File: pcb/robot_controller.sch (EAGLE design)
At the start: 93 parts, among them IC2 ESP32-DEVKIT, IC3 BTS7960B, IC4 BTS7960B, IC5 BTS7960B, IC6 BTS7960B, IC7 BTS7960B, IC8 BTS7960B, J6 1X2-3.5MM, Q1 IRLB8743

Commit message: update PCB to v1.1
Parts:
- added C43: (no value), rcl:CPOL-EUE5-10.5
- C42: value 10nF -> 100nF
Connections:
- removed net A13: IC2.D25
- removed net N$8: IC2.D35
- net GND: now also C43.-
- net VBATT: now also C43.+
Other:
- moved on the sheet: C42, R18, R20

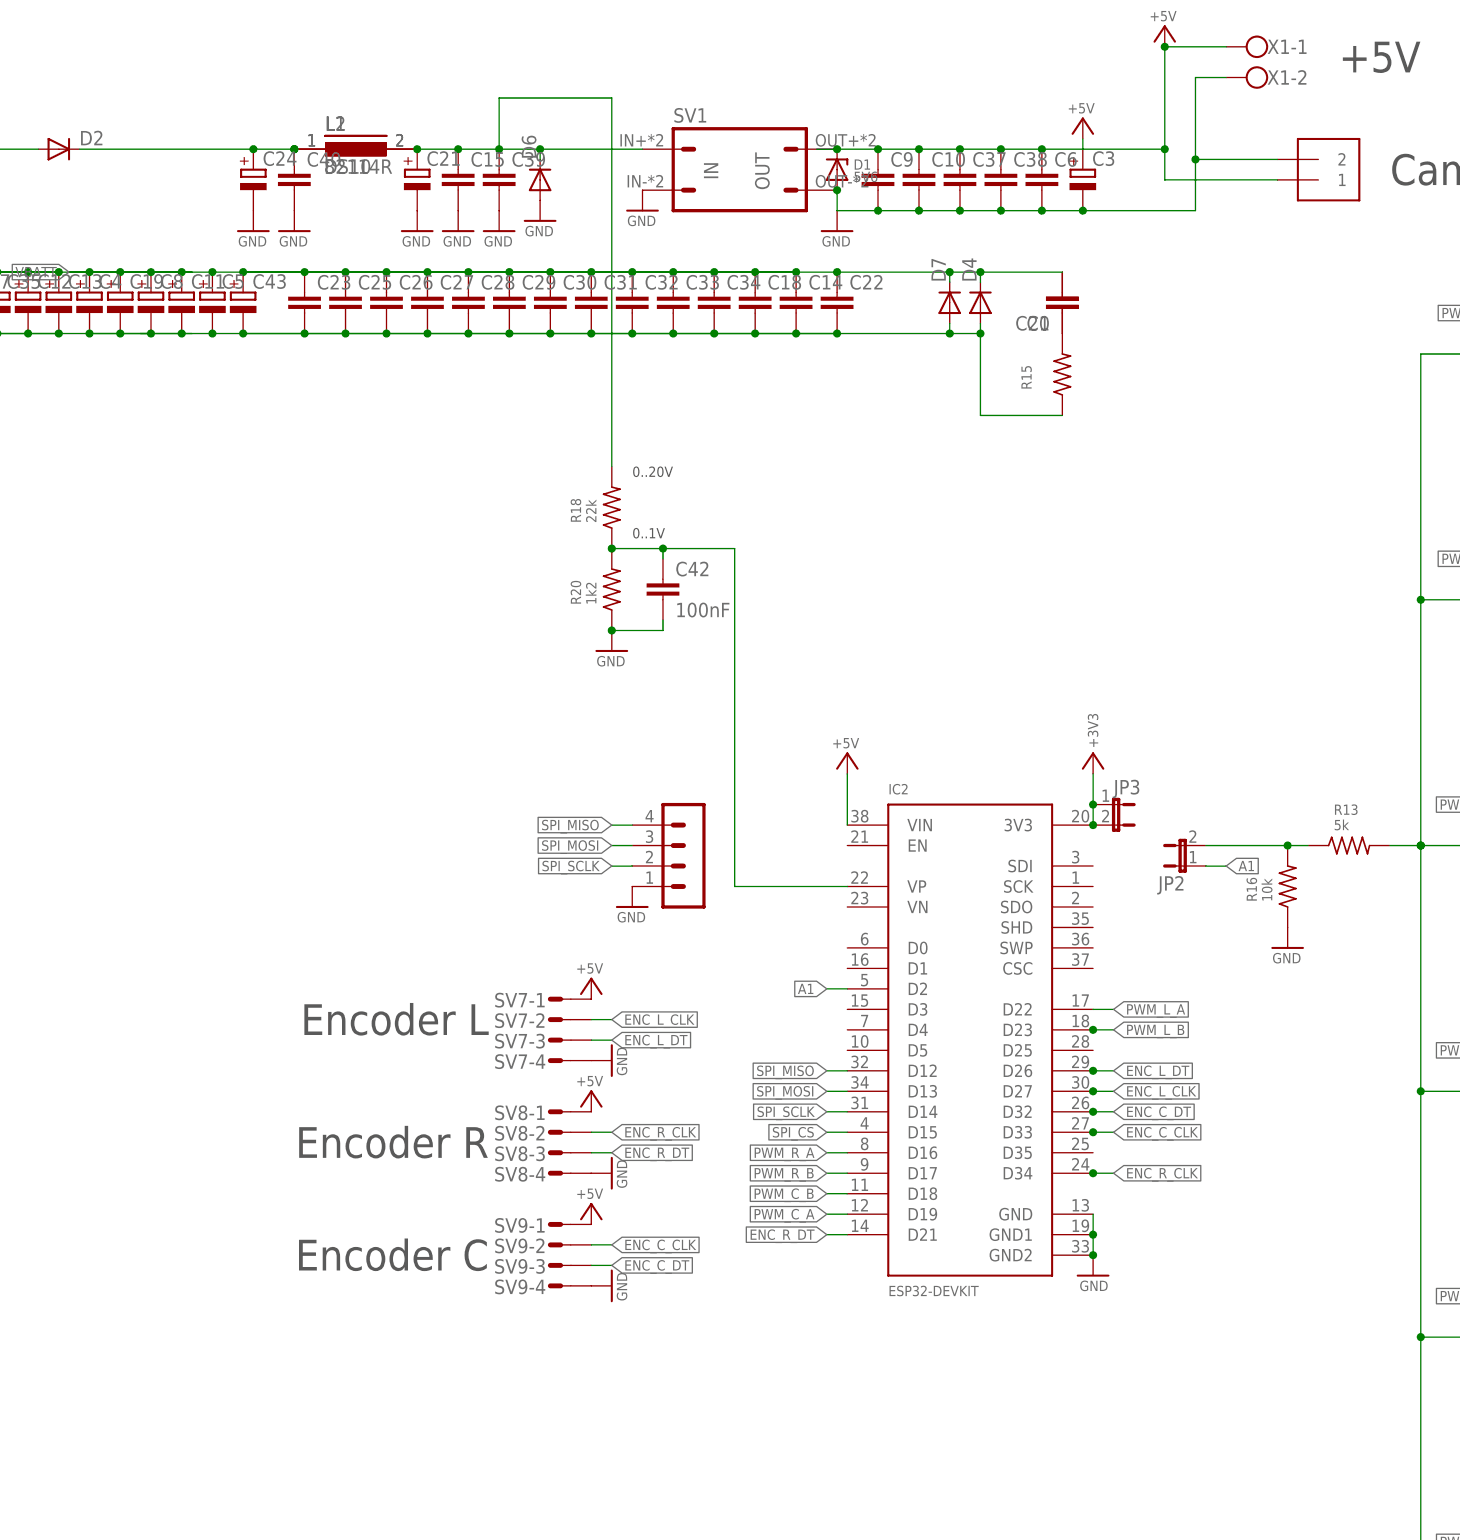
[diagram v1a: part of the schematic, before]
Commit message: update PCB and gerbers for v1.1
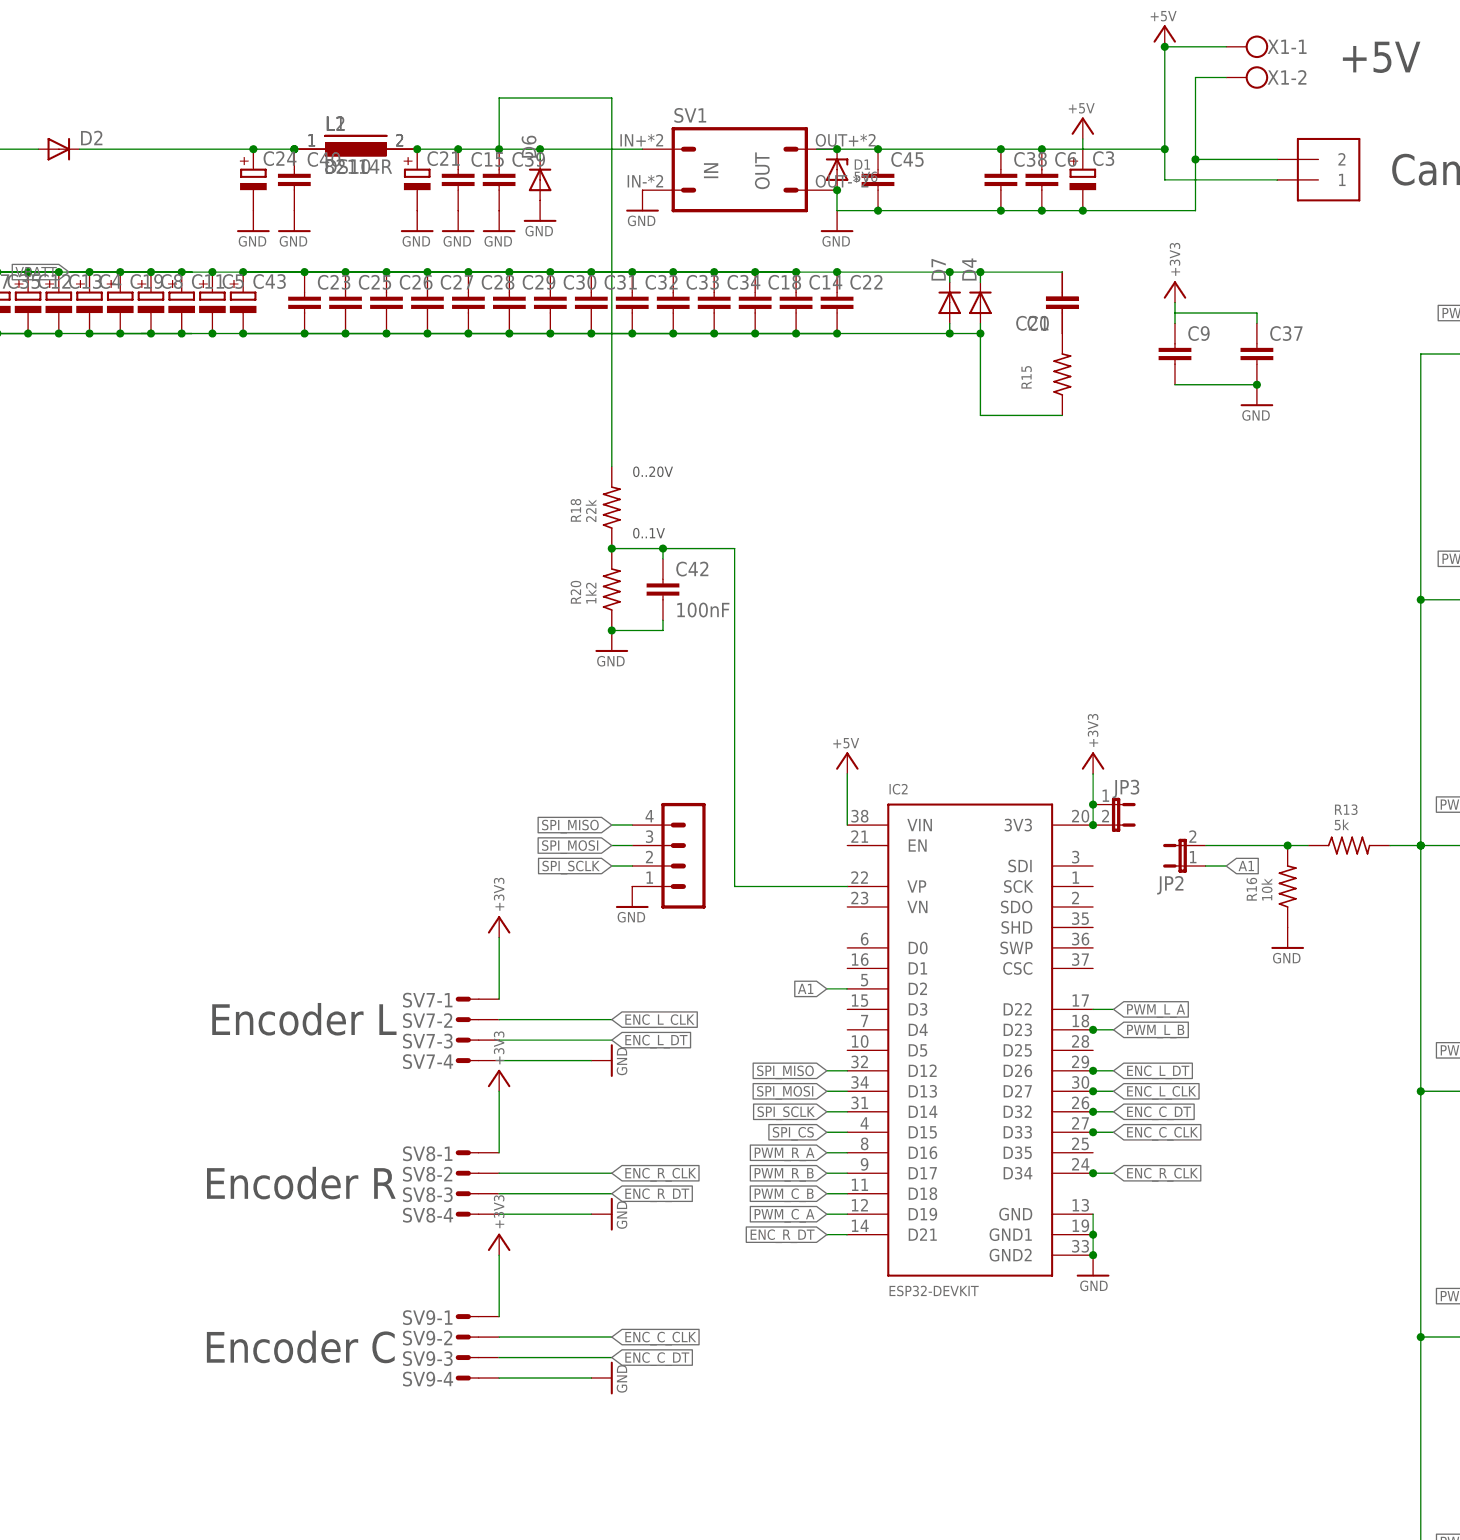
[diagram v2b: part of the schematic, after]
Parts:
- removed C10: (no value), rcl:C-EUC1206
- added C45: (no value), rcl:C-EUC1206
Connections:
- net +3V3: now also C37.1, C9.1, SV7-1.S, SV8-1.S, SV9-1.S
- net +5V: now also C45.1; no longer C10.1, C37.1, C9.1, SV7-1.S, SV8-1.S, SV9-1.S
- net GND: now also C45.2; no longer C10.2
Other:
- moved on the sheet: C37, C9, SV7-1, SV7-2, SV7-3, SV7-4, SV8-1, SV8-2, SV8-3, SV8-4, SV9-1, SV9-2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

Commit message: add jumpers to the PCB for setting the address
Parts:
- added JP_A0, JP_A1: (no value), jumper:JP1E
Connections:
- new net N$29: IC2.D35, JP_A0.2
- new net N$8: IC2.D25, JP_A1.2
- net GND: now also JP_A0.1, JP_A1.1
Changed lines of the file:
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@@
 <part name="C45" library="rcl" deviceset="C-EU" device="C1206"/>
 <part name="GND15" library="supply1" deviceset="GND" device=""/>
+<part name="JP_A1" library="jumper" deviceset="JP1E" device=""/>
+<part name="GND31" library="supply1" deviceset="GND" device=""/>
+<part name="JP_A0" library="jumper" deviceset="JP1E" device=""/>
+<part name="GND32" library="supply1" deviceset="GND" device=""/>
 </parts>
 <sheets>
@@
 <instance part="GND15" gate="1" x="36.83" y="171.45" smashed="yes">
 <attribute name="VALUE" x="34.925" y="169.545" size="1.27" layer="96" font="vector" ratio="18"/>
+</instance>
+<instance part="JP_A1" gate="A" x="41.91" y="88.9" rot="R180"/>
+<instance part="GND31" gate="1" x="41.91" y="93.98" smashed="yes" rot="R180">
+<attribute name="VALUE" x="43.815" y="95.885" size="1.27" layer="96" font="vector" ratio="18" rot="R180"/>
+</instance>
+<instance part="JP_A0" gate="A" x="41.91" y="76.2" rot="R180"/>
+<instance part="GND32" gate="1" x="41.91" y="81.28" smashed="yes" rot="R180">
+<attribute name="VALUE" x="43.815" y="83.185" size="1.27" layer="96" font="vector" ratio="18" rot="R180"/>
 </instance>
 </instances>
@@
 <wire x1="-36.83" y1="143.51" x2="-36.83" y2="144.78" width="0.1524" layer="91"/>
 <junction x="-43.18" y="143.51"/>
+</segment>
+<segment>
+<pinref part="JP_A1" gate="A" pin="1"/>
+<pinref part="GND31" gate="1" pin="GND"/>
+</segment>
+<segment>
+<pinref part="JP_A0" gate="A" pin="1"/>
+<pinref part="GND32" gate="1" pin="GND"/>
 </segment>
 </net>
@@
 </segment>
 </net>
+<net name="N$8" class="0">
+<segment>
+<pinref part="IC2" gate="G$1" pin="D25"/>
+<wire x1="16.51" y1="91.44" x2="39.37" y2="91.44" width="0.1524" layer="91"/>
+<pinref part="JP_A1" gate="A" pin="2"/>
+</segment>
+</net>
+<net name="N$29" class="0">
+<segment>
+<pinref part="IC2" gate="G$1" pin="D35"/>
+<pinref part="JP_A0" gate="A" pin="2"/>
+<wire x1="16.51" y1="78.74" x2="39.37" y2="78.74" width="0.1524" layer="91"/>
+</segment>
+</net>

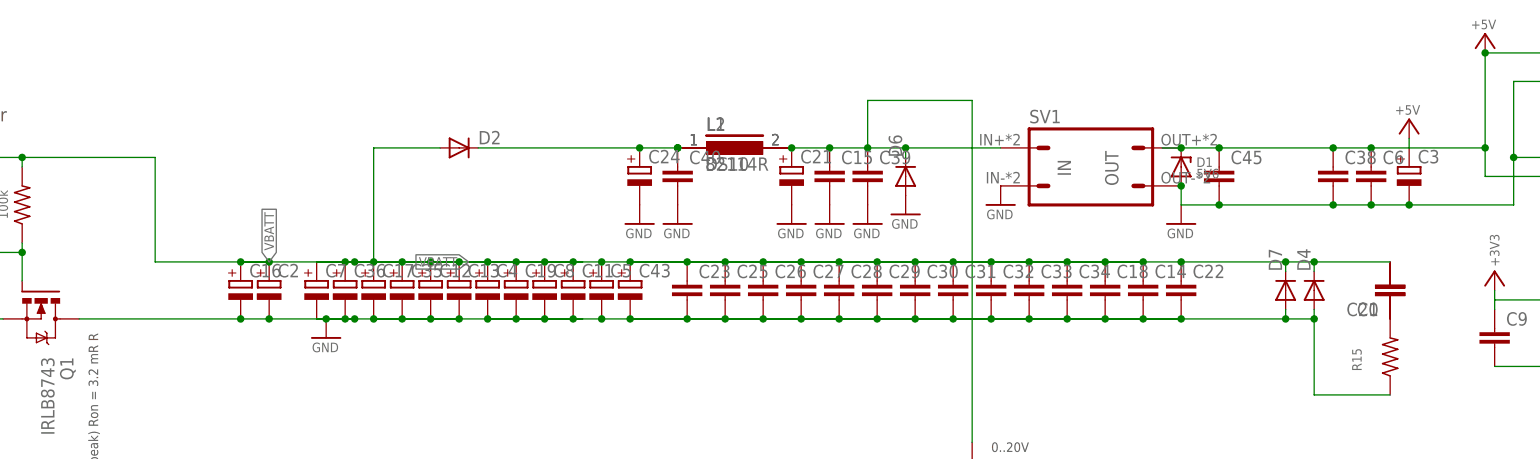
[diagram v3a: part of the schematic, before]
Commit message: add GND and +12V tap points to the controller PCB
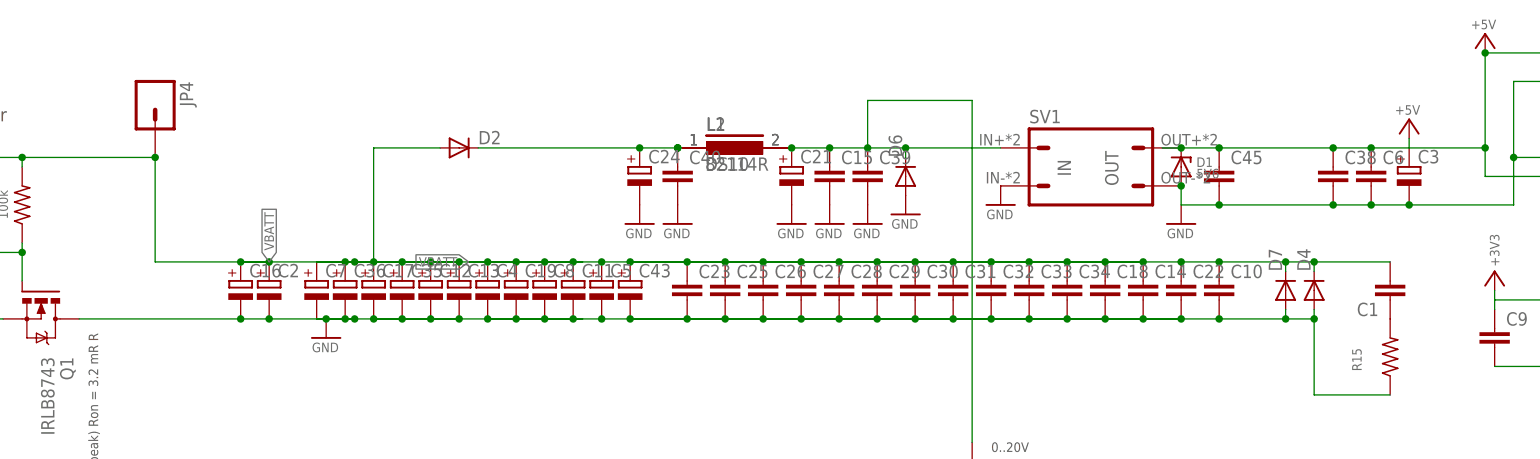
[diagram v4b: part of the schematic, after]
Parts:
- removed C20: (no value), rcl:C-EU050-030X075
- added C10: (no value), rcl:C-EUC1206
- added JP4: M01PTH_LONGPAD, SparkFun:M01PTH_LONGPAD
- C1: device rcl:C-EU050-030X075 -> rcl:C-EU025-025X050
- R15: device rcl:R-US_0617/5V -> rcl:R-US_0411/3V
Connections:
- net GND: now also C10.2
- net N$26: no longer C20.1
- net VBATT: now also C10.1, JP4.1; no longer C20.2
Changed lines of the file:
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@@
 <setting verticaltext="up"/>
 </settings>
-<grid distance="0.05" unitdist="inch" unit="inch" style="lines" multiple="1" display="yes" altdistance="0.01" altunitdist="inch" altunit="inch"/>
+<grid distance="0.05" unitdist="inch" unit="inch" style="lines" multiple="1" display="no" altdistance="0.01" altunitdist="inch" altunit="inch"/>
 <layers>
 <layer number="1" name="Top" color="4" fill="1" visible="no" active="no"/>
@@
 <part name="C24" library="rcl" deviceset="CPOL-EU" device="E5-10.5"/>
 <part name="GND27" library="supply1" deviceset="GND" device=""/>
-<part name="R15" library="rcl" deviceset="R-US_" device="0617/5V"/>
-<part name="C20" library="rcl" deviceset="C-EU" device="050-030X075"/>
-<part name="C1" library="rcl" deviceset="C-EU" device="050-030X075"/>
+<part name="R15" library="rcl" deviceset="R-US_" device="0411/3V"/>
+<part name="C1" library="rcl" deviceset="C-EU" device="025-025X050"/>
 <part name="R16" library="rcl" deviceset="R-US_" device="R1206" value="10k"/>
 <part name="GND29" library="supply1" deviceset="GND" device=""/>
@@
 <part name="JP_A0" library="jumper" deviceset="JP1E" device=""/>
 <part name="GND32" library="supply1" deviceset="GND" device=""/>
+<part name="C10" library="rcl" deviceset="C-EU" device="C1206"/>
+<part name="JP4" library="SparkFun" deviceset="M01" device="PTH_LONGPAD"/>
 </parts>
 <sheets>
@@
 </instance>
 <instance part="R15" gate="G$1" x="12.7" y="175.26" rot="R90"/>
-<instance part="C20" gate="G$1" x="12.7" y="182.88" rot="R180"/>
 <instance part="C1" gate="G$1" x="12.7" y="182.88" rot="R180"/>
 <instance part="R16" gate="G$1" x="40.64" y="111.76" rot="R90"/>
@@
 <instance part="GND32" gate="1" x="41.91" y="81.28" smashed="yes" rot="R180">
 <attribute name="VALUE" x="43.815" y="83.185" size="1.27" layer="96" font="vector" ratio="18" rot="R180"/>
+</instance>
+<instance part="C10" gate="G$1" x="-10.16" y="185.42"/>
+<instance part="JP4" gate="G$1" x="-152.4" y="209.55" smashed="yes" rot="R270">
+<attribute name="NAME" x="-149.098" y="212.09" size="1.778" layer="95" rot="R270"/>
 </instance>
 </instances>
@@
 <pinref part="C2" gate="G$1" pin="-"/>
 <wire x1="-25.4" y1="180.34" x2="-20.32" y2="180.34" width="0.1524" layer="91"/>
-<wire x1="-20.32" y1="180.34" x2="-1.27" y2="180.34" width="0.1524" layer="91"/>
+<wire x1="-20.32" y1="180.34" x2="-10.16" y2="180.34" width="0.1524" layer="91"/>
+<wire x1="-10.16" y1="180.34" x2="-1.27" y2="180.34" width="0.1524" layer="91"/>
 <wire x1="-1.27" y1="180.34" x2="2.54" y2="180.34" width="0.1524" layer="91"/>
 <wire x1="12.7" y1="170.18" x2="2.54" y2="170.18" width="0.1524" layer="91"/>
@@
 <pinref part="C43" gate="G$1" pin="-"/>
 <junction x="-88.9" y="180.34"/>
+<pinref part="C10" gate="G$1" pin="2"/>
+<junction x="-10.16" y="180.34"/>
 </segment>
 <segment>
@@
 <junction x="-125.73" y="187.96"/>
 <pinref part="D2" gate="G$1" pin="A"/>
-<pinref part="C20" gate="G$1" pin="2"/>
-<wire x1="-15.24" y1="187.96" x2="-1.27" y2="187.96" width="0.1524" layer="91"/>
+<wire x1="-15.24" y1="187.96" x2="-10.16" y2="187.96" width="0.1524" layer="91"/>
 <pinref part="C1" gate="G$1" pin="2"/>
+<wire x1="-10.16" y1="187.96" x2="-1.27" y2="187.96" width="0.1524" layer="91"/>
 <wire x1="2.54" y1="187.96" x2="12.7" y2="187.96" width="0.1524" layer="91"/>
 <junction x="-92.71" y="187.96"/>
@@
 <pinref part="C43" gate="G$1" pin="+"/>
 <junction x="-88.9" y="187.96"/>
+<pinref part="C10" gate="G$1" pin="1"/>
+<junction x="-10.16" y="187.96"/>
+<pinref part="JP4" gate="G$1" pin="1"/>
+<junction x="-152.4" y="201.93"/>
 </segment>
 <segment>
@@
 <segment>
 <pinref part="R15" gate="G$1" pin="2"/>
-<pinref part="C20" gate="G$1" pin="1"/>
 <pinref part="C1" gate="G$1" pin="1"/>
 </segment>
